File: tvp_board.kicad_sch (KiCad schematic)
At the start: 107 parts, among them J1 VGA, J3 SCART-F, J5 5VDC_IN, J6 SJ1-3533NG, J7 SJ1-3533NG, Q3 AOSS21115C, Q4 DSS20200L, Q5 AOSS21115C, SW1 SPST, SW4 GW22RCV, U1 TVP7002PZP, U17 THS7353, U18 LM3671MF-2.5/NOPB, U4 SN74LVC2G17, U5 AP7361C

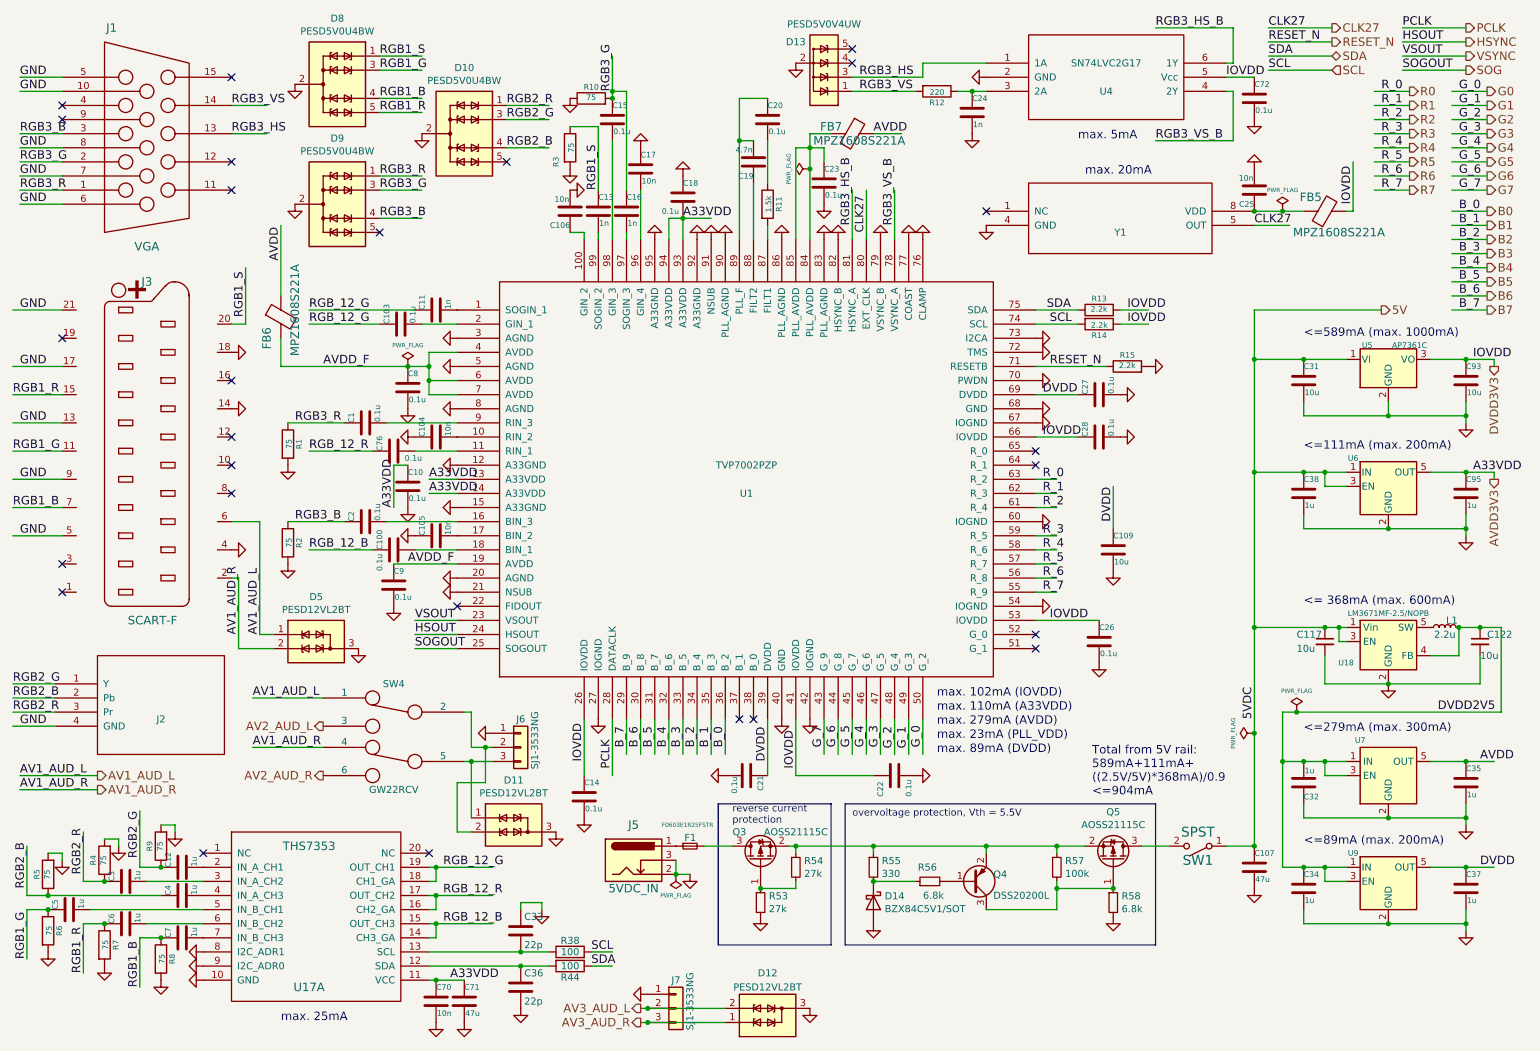
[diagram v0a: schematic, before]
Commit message: additional updates for PCB v1.8
* change to 4-layer stackup for better power delivery
* choose another FPGA pin for PCB version indicator
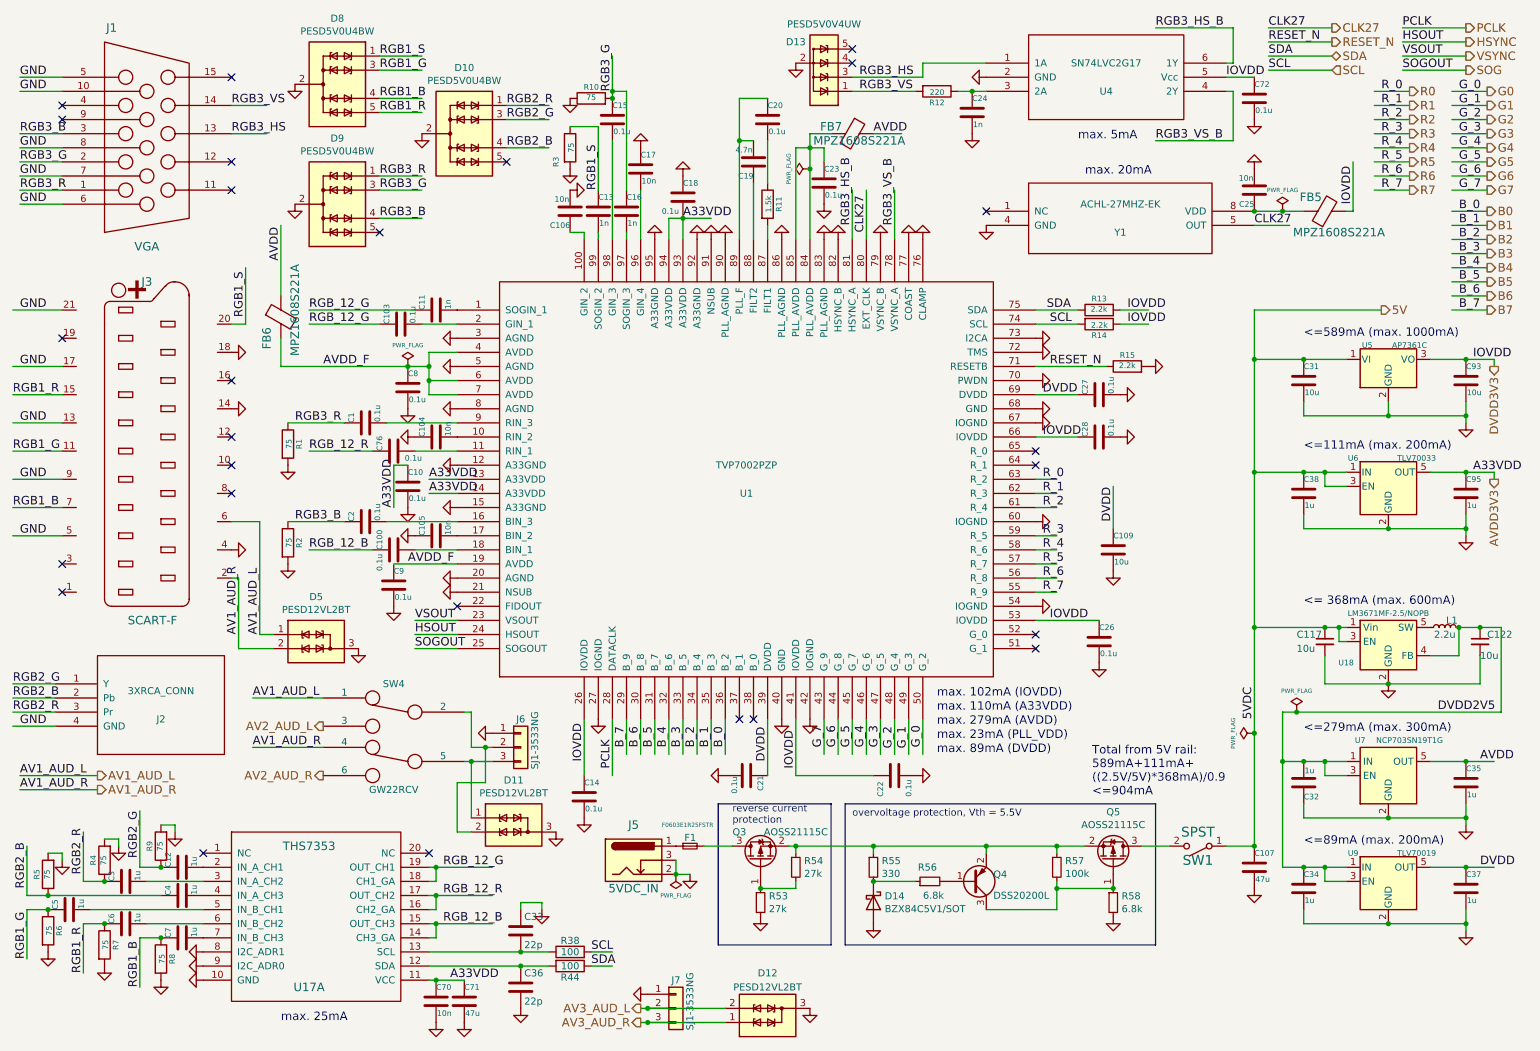
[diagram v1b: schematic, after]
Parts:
- J2: value (none) -> 3XRCA_CONN; footprint (none) -> custom_components:3xRCA_CONN
- U6: value (none) -> TLV70033; footprint (none) -> custom_components:SOT-23-5_Handsoldering
- U7: value (none) -> NCP703SN19T1G; footprint (none) -> custom_components:SOT-23-5_Handsoldering
- U9: value (none) -> TLV70019; footprint (none) -> custom_components:SOT-23-5_Handsoldering
- Y1: value (none) -> ACHL-27MHZ-EK; footprint (none) -> custom_components:ACHL-OSC
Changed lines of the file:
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@@
     (in_bom yes) (on_board yes)
     (property "Reference" "J2" (id 0) (at 40.64 139.7 0))
-    (property "Value" "" (id 1) (at 40.64 134.62 0))
-    (property "Footprint" "" (id 2) (at 40.64 137.16 0)
+    (property "Value" "3XRCA_CONN" (id 1) (at 40.64 134.62 0))
+    (property "Footprint" "custom_components:3xRCA_CONN" (id 2) (at 40.64 137.16 0)
       (effects (font (size 1.27 1.27)) hide)
     )
@@
       (effects (font (size 1.016 1.016)))
     )
-    (property "Value" "" (id 1) (at 266.7 163.83 0)
-      (effects (font (size 1.016 1.016)))
-    )
-    (property "Footprint" "" (id 2) (at 261.62 166.37 0)
+    (property "Value" "TLV70019" (id 1) (at 266.7 163.83 0)
+      (effects (font (size 1.016 1.016)))
+    )
+    (property "Footprint" "custom_components:SOT-23-5_Handsoldering" (id 2) (at 261.62 166.37 0)
       (effects (font (size 0.889 0.889) italic) hide)
     )
@@
     (in_bom yes) (on_board yes)
     (property "Reference" "Y1" (id 0) (at 213.36 52.07 0))
-    (property "Value" "" (id 1) (at 213.36 46.99 0))
-    (property "Footprint" "" (id 2) (at 213.36 49.53 0)
+    (property "Value" "ACHL-27MHZ-EK" (id 1) (at 213.36 46.99 0))
+    (property "Footprint" "custom_components:ACHL-OSC" (id 2) (at 213.36 49.53 0)
       (effects (font (size 1.27 1.27)) hide)
     )
@@
       (effects (font (size 1.016 1.016)))
     )
-    (property "Value" "" (id 1) (at 266.7 92.71 0)
-      (effects (font (size 1.016 1.016)))
-    )
-    (property "Footprint" "" (id 2) (at 261.62 95.25 0)
+    (property "Value" "TLV70033" (id 1) (at 266.7 92.71 0)
+      (effects (font (size 1.016 1.016)))
+    )
+    (property "Footprint" "custom_components:SOT-23-5_Handsoldering" (id 2) (at 261.62 95.25 0)
       (effects (font (size 0.889 0.889) italic) hide)
     )
@@
       (effects (font (size 1.016 1.016)))
     )
-    (property "Value" "" (id 1) (at 265.43 143.51 0)
-      (effects (font (size 1.016 1.016)))
-    )
-    (property "Footprint" "" (id 2) (at 261.62 146.05 0)
+    (property "Value" "NCP703SN19T1G" (id 1) (at 265.43 143.51 0)
+      (effects (font (size 1.016 1.016)))
+    )
+    (property "Footprint" "custom_components:SOT-23-5_Handsoldering" (id 2) (at 261.62 146.05 0)
       (effects (font (size 0.762 0.762) italic) hide)
     )
